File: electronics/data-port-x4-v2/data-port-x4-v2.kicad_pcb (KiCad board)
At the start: 4 copper layers, 100 x 70 mm, 275 parts, among them J1 LEAD, J101 PORT1, J102 PINS1, J2 SWD, J201 PORT2, J202 PINS2, J301 PORT3, J302 PINS3, J401 PORT4, J402 PINS4, Q1 2N7002, Q2 2N7002, Q3 2N7002, U1 USB2517I-JZX, U10 TCA9534APWR, U101 TPS2553DBVR-1, U102 INA226AIDGSR, U103 USBLC6-2SC6, U105 H5VU25UC, U106 H5VU25UC, U107 LSF0108RKSR, U108 H5VU25UC, U109 H5VU25UC, U11 RP2354B, U2 TCA6408ARGTR, U201 TPS2553DBVR-1, U202 INA226AIDGSR, U203 USBLC6-2SC6, U205 H5VU25UC, U206 H5VU25UC, U207 LSF0108RKSR, U208 H5VU25UC, U209 H5VU25UC, U3 AP2114H-3.3TRG1, U301 TPS2553DBVR-1, U302 INA226AIDGSR, U303 USBLC6-2SC6, U305 H5VU25UC, U306 H5VU25UC, U307 LSF0108RKSR, U308 H5VU25UC, U309 H5VU25UC, U4 H5VU25UC, U401 TPS2553DBVR-1, U402 INA226AIDGSR, U403 USBLC6-2SC6, U405 H5VU25UC, U406 H5VU25UC, U407 LSF0108RKSR, U408 H5VU25UC, U409 H5VU25UC, U5 MAX809S, U6 TCA6408ARGTR, U7 CH446Q, U8 CH446Q, U9 TPS60400DBVR, Y1 X322524MSB4SI, Y2 ABM8-272-T3

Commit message: DATA x4 v2: C29 turned, right west of the matrix expander's VDD
C29 (100 nF, +3V3) sat 2.62 mm below U10's VDD pin 16 (U10: the
TCA9534A driving the crosspoints), turned with its +3V3 pad down,
away from the pin.  It now stands right west of the pin, its +3V3 pad
up, 0.66 mm: VDD, then C29, then its via, drawn on F.Cu; its GND via
below it.

Routed incrementally: no other net rerouted (SCL and PORT4_CONN_DP
move by the tidy pass's 1-9 um).  In the SES, the router's TP29 stub
dropped.  ERC 0, DRC 0, unconnected 0, no antenna; panel DRC 0.  The
board stays pending in electronics/decoupling.json (11 left).

Co-Authored-By: Claude Opus 5.5 <noreply@anthropic.com>
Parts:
- moved C29 1.79 mm to (10.6, 5.30), turned to -90 degrees
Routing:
- net +3V3: track 71.6 -> 72.2 mm, vias 70 -> 69

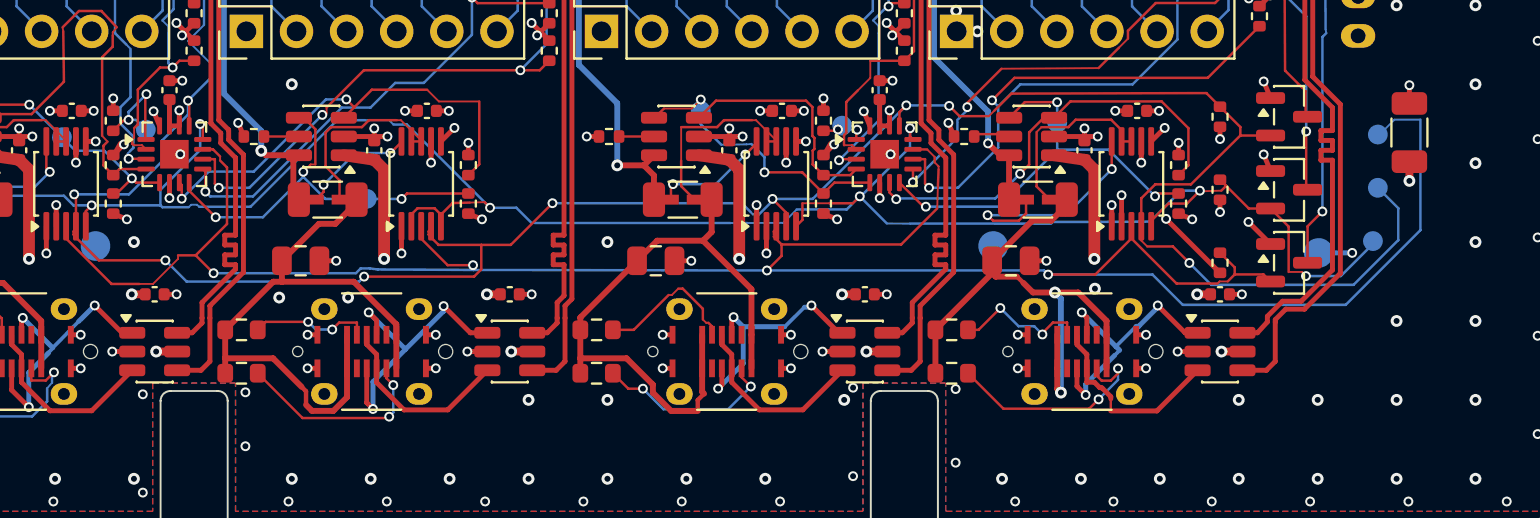
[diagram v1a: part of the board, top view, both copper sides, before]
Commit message: DATA x4 v2: each port's VBUS 100 nF right over its ESD, fed between its pin rows
C104-C404 (100 nF, +5V) sat 2.39 mm north of their USBLC6's VBUS pin
5, which each port's D+/D- walls in on its east; pin 5 took its via
west, under the ESD's body.  Each capacitor now stands right over the
ESD, its +5V pad above the gap between the two pin rows (0.95 mm),
1.70 mm from the pin: VBUS runs west under the body, up that gap to the
capacitor, then on to its via (pin, capacitor, via, drawn on F.Cu, the
same on all four ports); its GND via beside it.

Routed incrementally: INT's B.Cu jog under port 4 moves 1.5 mm east
round C404's GND via (same length); SCL and PORT4_CONN_DP move by the
tidy pass's 1-9 um.  In the SES, the router's CP_SWDIO double, TP29
stub and second CP_SNS_5V link dropped.  ERC 0, DRC 0, unconnected 0,
no antenna; panel DRC 0.  The board stays pending in
electronics/decoupling.json (7 left).

Co-Authored-By: Claude Opus 5.5 <noreply@anthropic.com>
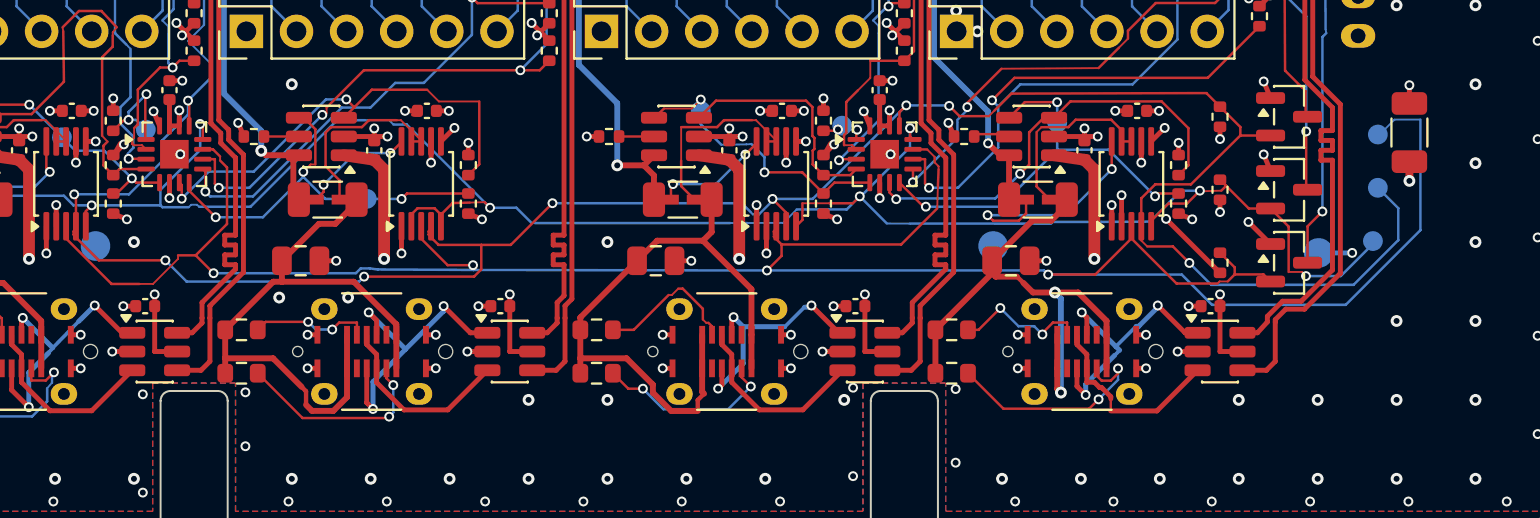
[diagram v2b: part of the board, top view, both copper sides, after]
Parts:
- moved C304 0.77 mm to (64.5, 59.2), turned to 180 degrees
- moved C404 0.77 mm to (82.5, 59.2), turned to 180 degrees
- moved C104 0.77 mm to (28.5, 59.2), turned to 180 degrees
- moved C204 0.77 mm to (46.5, 59.2), turned to 180 degrees
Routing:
- net +5V: track 41.7 -> 50.8 mm, vias 16 -> 12
- net GND: vias 373 -> 372
